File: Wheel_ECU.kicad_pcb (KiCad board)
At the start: 2 copper layers, 61 x 61 mm, 63 parts, among them J1 Conn_01x04, J2 Conn_01x04, J3 Conn_01x02, J4 Debug, J5 Conn_01x02, U1 IFX9201SG, U2 TLE4964, U3 XMC1404_F064, U4 TLE7251

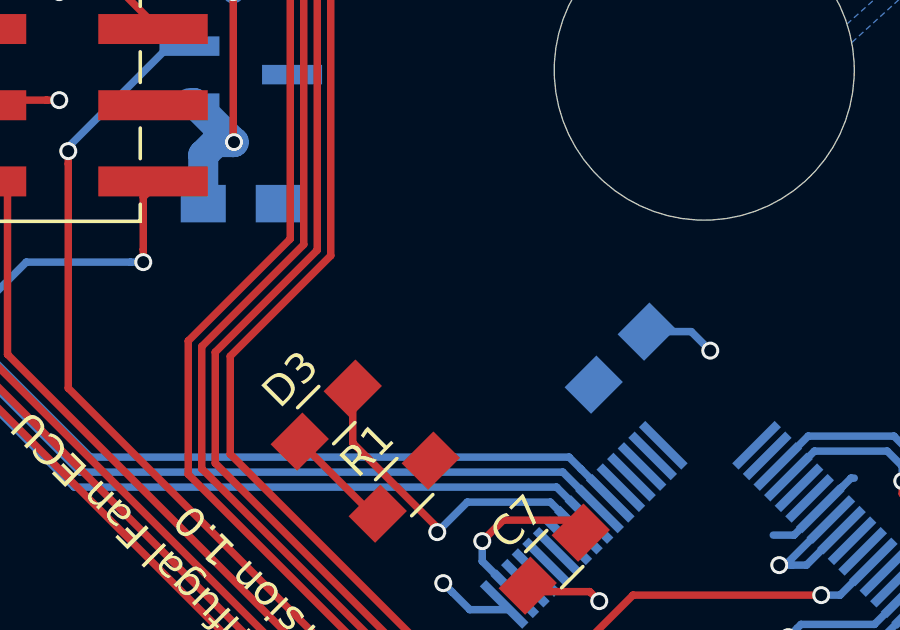
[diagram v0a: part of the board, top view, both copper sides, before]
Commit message: Add a temperature sensor (LM35D)
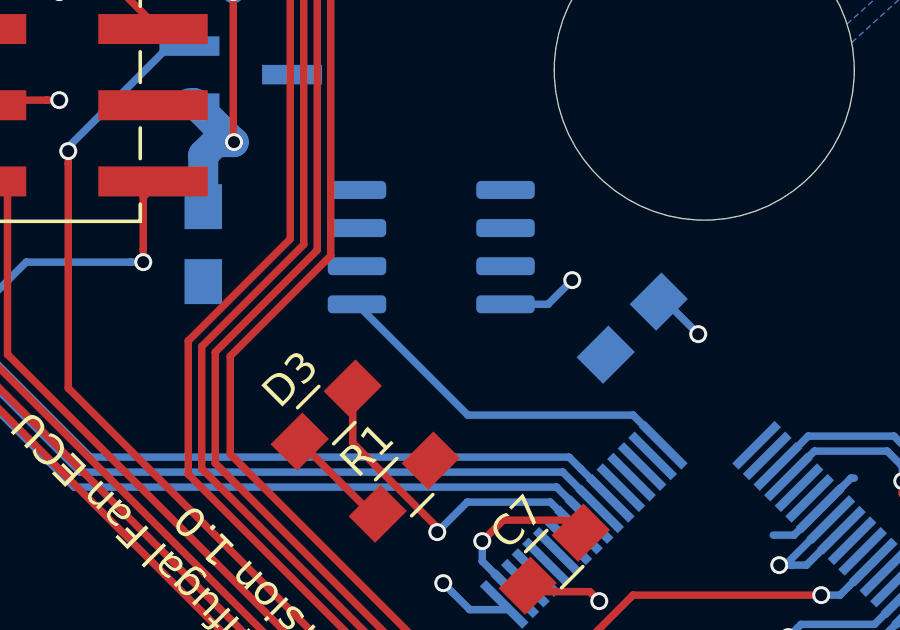
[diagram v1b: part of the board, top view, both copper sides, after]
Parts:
- added U5: LM35-D, Package_SO:SOIC-8_3.9x4.9mm_P1.27mm, B.Cu at (122.7, 104.3)
- moved C2 1.84 mm to (115.1, 104.2), turned to 90 degrees
- moved C8 1.08 mm to (129.4, 107.0)
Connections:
- U3 pad 16: Net-(U3-Pad16) -> TEMP_SENSOR_OUTPUT
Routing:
- net TEMP_SENSOR_OUTPUT: track 0.00 -> 12.2 mm
- net +5V: track 57.1 -> 59.1 mm, vias 13 -> 14
